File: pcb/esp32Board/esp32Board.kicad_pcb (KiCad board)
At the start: 4 copper layers, 38.2 x 42.1 mm, 31 parts, among them J1 ESPProgJTAG_RX, J10 USB_C_Receptacle_USB2.0, J2 ESPProg_RX, J3 ESPProgUART_RX, J4 CAN, J5 UART2, J6 I2C, J7 IO, J8 PWR, J9 GND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

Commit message: PCB Update
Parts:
- C2: value 20uF -> 22uF
- R2, R3, R8, R9: footprint Capacitor_SMD:C_0603_1608Metric -> Resistor_SMD:R_0603_1608Metric
- R4: value 2k -> 100k
- moved R1 0.94 mm to (145.2, 107.4)
- moved C2 0.49 mm to (145.2, 109.5)
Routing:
- net /EN: track 68.4 -> 84.0 mm
- net +3V3: track 93.0 -> 98.2 mm, vias 5 -> 4
- net GND: track 181.0 -> 181.6 mm

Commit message: Fix PCB Error
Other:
- board size 38.2 x 42.1 mm -> 38.2 x 41.1 mm
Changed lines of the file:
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@@
   (gr_line (start 146.4564 138.2522) (end 146.4564 142.5702) (layer "F.SilkS") (width 0.35))
   (gr_arc (start 138.8872 109.761573) (mid 140.058145 106.935942) (end 142.884027 105.7656) (layer "Edge.Cuts") (width 0.1))
-  (gr_line (start 177.0756 143.8728) (end 177.0756 109.743373) (layer "Edge.Cuts") (width 0.1))
+  (gr_line (start 177.0756 142.8728) (end 177.0756 109.743373) (layer "Edge.Cuts") (width 0.1))
   (gr_line (start 173.0756 105.743373) (end 142.884027 105.7656) (layer "Edge.Cuts") (width 0.1))
   (gr_arc (start 173.0756 105.743373) (mid 175.904027 106.914946) (end 177.0756 109.743373) (layer "Edge.Cuts") (width 0.1))
-  (gr_line (start 138.8872 109.761573) (end 138.8872 143.891) (layer "Edge.Cuts") (width 0.1))
-  (gr_arc (start 142.8872 147.891) (mid 140.058773 146.719427) (end 138.8872 143.891) (layer "Edge.Cuts") (width 0.1))
-  (gr_line (start 142.8872 147.891) (end 173.0756 147.8728) (layer "Edge.Cuts") (width 0.1))
-  (gr_arc (start 177.0756 143.8728) (mid 175.904027 146.701227) (end 173.0756 147.8728) (layer "Edge.Cuts") (width 0.1))
+  (gr_line (start 138.8872 109.761573) (end 138.8872 142.891) (layer "Edge.Cuts") (width 0.1))
+  (gr_arc (start 142.8872 146.891) (mid 140.058773 145.719427) (end 138.8872 142.891) (layer "Edge.Cuts") (width 0.1))
+  (gr_line (start 142.8872 146.891) (end 173.0756 146.8728) (layer "Edge.Cuts") (width 0.1))
+  (gr_arc (start 177.0756 142.8728) (mid 175.904027 145.701227) (end 173.0756 146.8728) (layer "Edge.Cuts") (width 0.1))
   (gr_text "JLCJLCJLCJLC" (at 158.115 108.458) (layer "B.SilkS")
     (effects (font (size 1 1) (thickness 0.15)) (justify mirror))

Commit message: PCB V0.2
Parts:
- removed J2: ESPProg_RX, Connector_Molex:Molex_CLIK-Mate_502382-1070_1x10-1MP_P1.25mm_Vertical
- removed R9: 0, Resistor_SMD:R_0603_1608Metric
- added D3: LED, LED_SMD:LED_0603_1608Metric, F.Cu at (146.1, 126.0)
- added J11: Conn_01x14_Female, Connector_PinHeader_2.54mm:PinHeader_1x14_P2.54mm_Vertical, F.Cu at (172.5, 108.8)
- added SW2: SW_Push_SPDT, KisonNew:0603JumperP3, F.Cu at (151.2, 129.5)
- added SW3: SW_Push_SPDT, KisonNew:0603JumperP3, F.Cu at (162.7, 133.4)
- added SW4: SW_Push_SPDT, KisonNew:0603JumperP3, F.Cu at (154.4, 129.3)
- J7: value IO -> InputOnly; footprint Connector_PinHeader_2.54mm:PinHeader_1x08_P2.54mm_Vertical -> Connector_PinHeader_2.54mm:PinHeader_1x04_P2.54mm_Vertical
- R4: value 100k -> 10k; moved to B.Cu
- R8: value 0 -> 10k; moved to B.Cu
- moved J7 32.2 mm to (142.1, 119.8), turned to 180 degrees
- moved J3 26.2 mm to (163.3, 109.8), turned to 180 degrees
- moved R8 25.4 mm to (143.3, 123.4), turned to -90 degrees
- moved J6 19.1 mm to (146.1, 119.0), turned to 0 degrees
- moved R4 18.4 mm to (141.5, 123.4), turned to -90 degrees
- moved D2 11.8 mm to (148.9, 132.2), turned to 180 degrees
- moved D1 10.3 mm to (146.1, 127.7)
- moved SW1 8.89 mm to (142.1, 128.3), turned to -90 degrees
- moved G*** 8.88 mm to (150.0, 131.5), turned to 0 degrees
- moved J1 8.78 mm to (150.9, 109.8), turned to 180 degrees
- moved C4 8.44 mm to (142.4, 128.6), turned to 0 degrees
- moved C6 8.17 mm to (159.5, 133.2), turned to -90 degrees
- moved R5 8.16 mm to (155.8, 145.0), turned to 0 degrees
- moved J8 7.27 mm to (144.0, 144.8), turned to 180 degrees
- moved R6 7.16 mm to (153.6, 141.6), turned to 0 degrees
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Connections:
- J4 pad 1: /CAN_VCC -> Net-(J4-Pad1)
- J7 pad 1: /IO23 -> /IO35
- J7 pad 2: /IO19 -> /IO34
- J7 pad 3: /IO18 -> /IO39
- J7 pad 4: /IO5 -> /IO36
- R8 pad 2: /CAN_VCC -> Net-(D3-Pad2)
- U1 pad 4: unconnected-(U1-Pad4) -> /IO36
- U1 pad 5: unconnected-(U1-Pad5) -> /IO39
- U1 pad 7: unconnected-(U1-Pad7) -> /IO35
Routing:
- net /EN: track 84.0 -> 46.4 mm, vias 3 -> 2
- net Net-(J11-Pad14): track 0.00 -> 26.5 mm, vias 0 -> 1
- net /IO5: track 6.75 -> 32.0 mm
- net /IO0: track 39.0 -> 14.0 mm
- net /RX: track 31.6 -> 9.22 mm, vias 2 -> 0
- net /EXT_5V: track 24.9 -> 46.2 mm, vias 0 -> 1
- net /TX: track 29.9 -> 12.3 mm, vias 2 -> 0
- net /SDA_IO25: track 20.9 -> 3.60 mm, vias 1 -> 0
- net /IO34: track 26.1 -> 8.95 mm, vias 1 -> 0
- net Net-(J4-Pad1): track 0.00 -> 16.0 mm, vias 0 -> 1
- net /TCLK: track 29.9 -> 15.2 mm, vias 2 -> 1
- net Net-(J11-Pad7): track 0.00 -> 13.9 mm, vias 0 -> 1
- net /SCL_IO26: track 18.0 -> 4.13 mm, vias 1 -> 0
- net /TMS: track 27.2 -> 14.2 mm, vias 2 -> 1
- net /IO32: track 24.4 -> 37.0 mm
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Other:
- board text added: "35"
- board text added: "36"
- board text added: "39"
- board text added: "GPPCB-V0.2"
- board text added: "InputOnly"
- board text added: "LED"
- board text added: "RX22"
- board text added: "TX21"
- board text added: "VCC"
- board text added: "屏幕朝向"
- board text removed: "RX_22"
- board text removed: "TX_21"

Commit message: Use XC6209 instead of trash XC6206
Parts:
- removed C6: 1uf, Capacitor_SMD:C_0603_1608Metric
- removed U2: XC6206P332MR, Package_TO_SOT_SMD:SOT-23
- added C10: 1uf, Capacitor_SMD:C_0603_1608Metric, F.Cu at (159.4, 133.3)
- added U3: XC6209, Package_TO_SOT_SMD:SOT-23-5, F.Cu at (156.2, 133.5)
- moved C5 0.59 mm to (153.1, 133.5)
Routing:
- net GND: track 175.5 -> 179.7 mm
- net /EXT_5V: track 46.2 -> 49.8 mm
- net Net-(D2-Pad2): track 18.2 -> 17.0 mm
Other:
- board text added: "GPPCB-V0.3"
- board text removed: "GPPCB-V0.2"

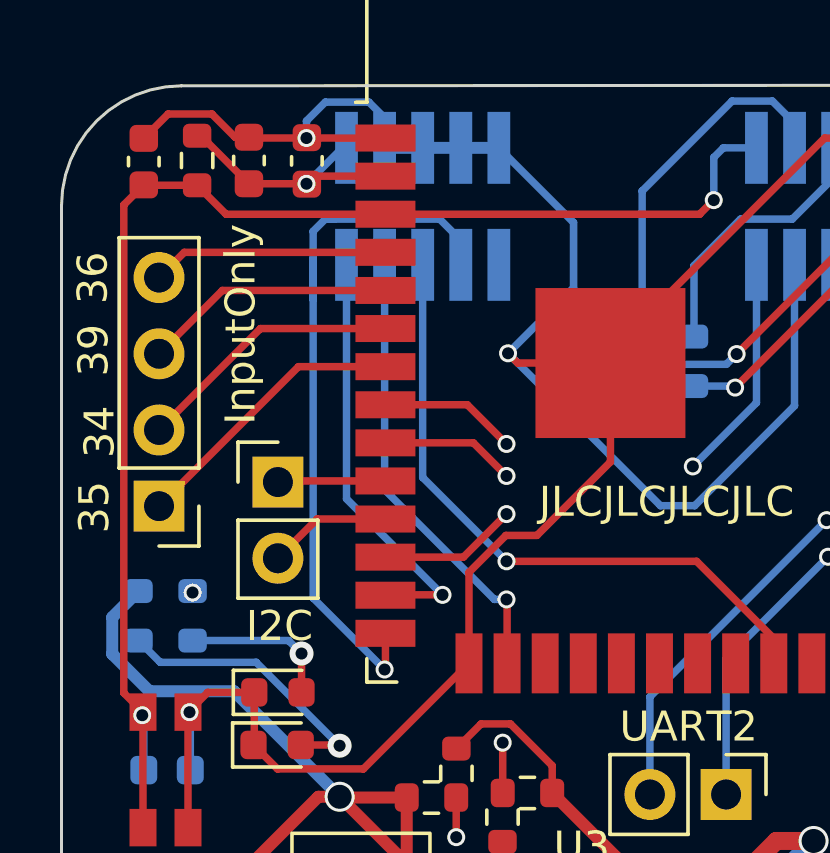
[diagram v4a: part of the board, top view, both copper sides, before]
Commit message: Fix I2C Pull Up
https://github.com/espressif/arduino-esp32/issues/3424 Damn why not design it strong enough so bad
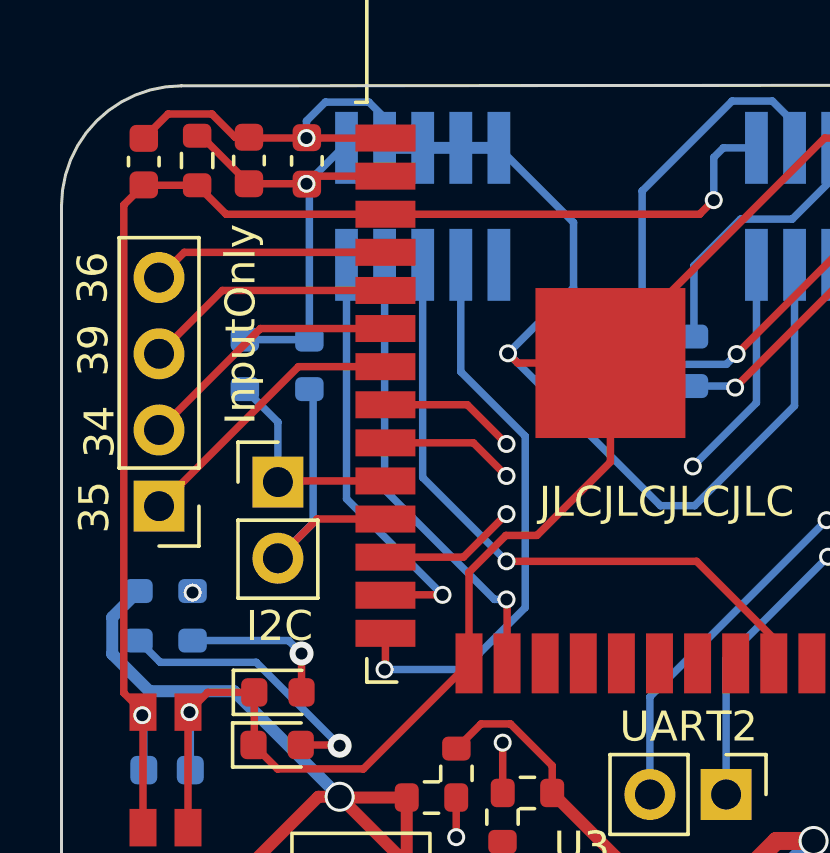
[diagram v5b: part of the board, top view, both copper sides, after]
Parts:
- added R10: 3.3k, Resistor_SMD:R_0603_1608Metric, B.Cu at (147.2, 115.0)
- added R9: 3.3k, Resistor_SMD:R_0603_1608Metric, B.Cu at (145.0, 115.0)
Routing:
- net +3V3: track 104.4 -> 111.8 mm
- net /SCL_IO26: track 4.13 -> 10.3 mm
- net /TDI: track 24.5 -> 19.9 mm
- net /SDA_IO25: track 3.60 -> 7.15 mm
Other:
- board text added: "GPPCB-V0.4"
- board text removed: "GPPCB-V0.3"
- board text removed: "屏幕朝向"
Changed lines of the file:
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@@
   )
   (footprint "Resistor_SMD:R_0603_1608Metric" (layer "B.Cu")
+    (at 145 115.05 -90)
+    (descr "Resistor SMD 0603 (1608 Metric), square (rectangular) end terminal, IPC_7351 nominal, (Body size source: IPC-SM-782 page 72, https://www.pcb-3d.com/wordpress/wp-content/uploads/ipc-sm-782a_amendment_1_and_2.pdf), generated with kicad-footprint-generator")
+    (tags "resistor")
+    (property "LCSC" "C429617")
+    (property "Sheetfile" "esp32Board.kicad_sch")
+    (property "Sheetname" "")
+    (attr smd)
+    (fp_text reference "R9" (at 0 1.43 90) (layer "B.SilkS")
+      (effects (font (size 1 1) (thickness 0.15)) (justify mirror))
+    )
+    (fp_text value "3.3k" (at 0 -1.43 90) (layer "B.Fab")
+      (effects (font (size 1 1) (thickness 0.15)) (justify mirror))
+    )
+    (fp_text user "${REFERENCE}" (at 0 0 90) (layer "B.Fab")
+      (effects (font (size 0.4 0.4) (thickness 0.06)) (justify mirror))
+    )
+    (fp_line (start -0.237258 0.5225) (end 0.237258 0.5225) (layer "B.SilkS") (width 0.12))
+    (fp_line (start -0.237258 -0.5225) (end 0.237258 -0.5225) (layer "B.SilkS") (width 0.12))
+    (fp_line (start 1.48 -0.73) (end -1.48 -0.73) (layer "B.CrtYd") (width 0.05))
+    (fp_line (start -1.48 -0.73) (end -1.48 0.73) (layer "B.CrtYd") (width 0.05))
+    (fp_line (start -1.48 0.73) (end 1.48 0.73) (layer "B.CrtYd") (width 0.05))
+    (fp_line (start 1.48 0.73) (end 1.48 -0.73) (layer "B.CrtYd") (width 0.05))
+    (fp_line (start -0.8 -0.4125) (end -0.8 0.4125) (layer "B.Fab") (width 0.1))
+    (fp_line (start 0.8 -0.4125) (end -0.8 -0.4125) (layer "B.Fab") (width 0.1))
+    (fp_line (start -0.8 0.4125) (end 0.8 0.4125) (layer "B.Fab") (width 0.1))
+    (fp_line (start 0.8 0.4125) (end 0.8 -0.4125) (layer "B.Fab") (width 0.1))
+    (pad "1" smd roundrect (at -0.825 0 270) (size 0.8 0.95) (layers "B.Cu" "B.Paste" "B.Mask") (roundrect_rratio 0.25)
+      (net 3 "+3V3") (pintype "passive"))
+    (pad "2" smd roundrect (at 0.825 0 270) (size 0.8 0.95) (layers "B.Cu" "B.Paste" "B.Mask") (roundrect_rratio 0.25)
+      (net 47 "/SDA_IO25") (pintype "passive"))
+    (model "${KICAD6_3DMODEL_DIR}/Resistor_SMD.3dshapes/R_0603_1608Metric.wrl"
+      (offset (xyz 0 0 0))
+      (scale (xyz 1 1 1))
+      (rotate (xyz 0 0 0))
+    )
+  )
+  (footprint "Resistor_SMD:R_0603_1608Metric" (layer "B.Cu")
     (at 155.8036 144.9832)
     (descr "Resistor SMD 0603 (1608 Metric), square (rectangular) end terminal, IPC_7351 nominal, (Body size source: IPC-SM-782 page 72, https://www.pcb-3d.com/wordpress/wp-content/uploads/ipc-sm-782a_amendment_1_and_2.pdf), generated with kicad-footprint-generator")
@@
       ) (layer "B.SilkS") (width 0) (fill solid))
   )
+  (footprint "Resistor_SMD:R_0603_1608Metric" (layer "B.Cu")
+    (at 147.15 115.05 -90)
+    (descr "Resistor SMD 0603 (1608 Metric), square (rectangular) end terminal, IPC_7351 nominal, (Body size source: IPC-SM-782 page 72, https://www.pcb-3d.com/wordpress/wp-content/uploads/ipc-sm-782a_amendment_1_and_2.pdf), generated with kicad-footprint-generator")
+    (tags "resistor")
+    (property "LCSC" "C429617")
+    (property "Sheetfile" "esp32Board.kicad_sch")
+    (property "Sheetname" "")
+    (attr smd)
+    (fp_text reference "R10" (at 0 1.43 90) (layer "B.SilkS")
+      (effects (font (size 1 1) (thickness 0.15)) (justify mirror))
+    )
+    (fp_text value "3.3k" (at 0 -1.43 90) (layer "B.Fab")
+      (effects (font (size 1 1) (thickness 0.15)) (justify mirror))
+    )
+    (fp_text user "${REFERENCE}" (at 0 0 90) (layer "B.Fab")
+      (effects (font (size 0.4 0.4) (thickness 0.06)) (justify mirror))
+    )
+    (fp_line (start -0.237258 -0.5225) (end 0.237258 -0.5225) (layer "B.SilkS") (width 0.12))
+    (fp_line (start -0.237258 0.5225) (end 0.237258 0.5225) (layer "B.SilkS") (width 0.12))
+    (fp_line (start -1.48 0.73) (end 1.48 0.73) (layer "B.CrtYd") (width 0.05))
+    (fp_line (start -1.48 -0.73) (end -1.48 0.73) (layer "B.CrtYd") (width 0.05))
+    (fp_line (start 1.48 0.73) (end 1.48 -0.73) (layer "B.CrtYd") (width 0.05))
+    (fp_line (start 1.48 -0.73) (end -1.48 -0.73) (layer "B.CrtYd") (width 0.05))
+    (fp_line (start -0.8 0.4125) (end 0.8 0.4125) (layer "B.Fab") (width 0.1))
+    (fp_line (start 0.8 -0.4125) (end -0.8 -0.4125) (layer "B.Fab") (width 0.1))
+    (fp_line (start 0.8 0.4125) (end 0.8 -0.4125) (layer "B.Fab") (width 0.1))
+    (fp_line (start -0.8 -0.4125) (end -0.8 0.4125) (layer "B.Fab") (width 0.1))
+    (pad "1" smd roundrect (at -0.825 0 270) (size 0.8 0.95) (layers "B.Cu" "B.Paste" "B.Mask") (roundrect_rratio 0.25)
+      (net 3 "+3V3") (pintype "passive"))
+    (pad "2" smd roundrect (at 0.825 0 270) (size 0.8 0.95) (layers "B.Cu" "B.Paste" "B.Mask") (roundrect_rratio 0.25)
+      (net 48 "/SCL_IO26") (pintype "passive"))
+    (model "${KICAD6_3DMODEL_DIR}/Resistor_SMD.3dshapes/R_0603_1608Metric.wrl"
+      (offset (xyz 0 0 0))
+      (scale (xyz 1 1 1))
+      (rotate (xyz 0 0 0))
+    )
+  )
   (footprint "KisonNew:IDC_1.27mm_10P" (layer "B.Cu")
     (at 150.9268 109.7832 180)
@@
     (effects (font (size 1 1) (thickness 0.15)) (justify mirror))
   )
-  (gr_text "屏幕朝向" (at 175.4124 122.4026 90) (layer "B.SilkS")
-    (effects (font (size 3 3) (thickness 0.15)) (justify mirror))
-  )
-  (gr_text "GPPCB-V0.3" (at 141.3002 140.0302 90) (layer "B.SilkS")
+  (gr_text "GPPCB-V0.4" (at 141.3002 140.0302 90) (layer "B.SilkS")
     (effects (font (size 1 1) (thickness 0.15)) (justify mirror))
   )
@@
   (segment (start 145.392911 135.800489) (end 144.0434 137.15) (width 0.6) (layer "B.Cu") (net 3))
   (segment (start 162.052 111.7332) (end 162.052 116.332) (width 0.25) (layer "B.Cu") (net 3))
+  (segment (start 147.15 109.1268) (end 147.053 109.0298) (width 0.25) (layer "B.Cu") (net 3))
+  (segment (start 147.15 114.225) (end 147.15 109.1268) (width 0.25) (layer "B.Cu") (net 3))
   (segment (start 163.957 130.937) (end 159.093511 135.800489) (width 0.6) (layer "B.Cu") (net 3))
   (segment (start 162.052 116.332) (end 159.9311 118.4529) (width 0.25) (layer "B.Cu") (net 3))
+  (segment (start 145 114.225) (end 147.15 114.225) (width 0.25) (layer "B.Cu") (net 3))
   (segment (start 148.2496 107.8332) (end 147.053 109.0298) (width 0.25) (layer "B.Cu") (net 3))
   (segment (start 144.0434 139.69) (end 144.0434 137.15) (width 1) (layer "B.Cu") (net 3))
@@
   (segment (start 149.685 124.0164) (end 149.685 125.1938) (width 0.25) (layer "F.Cu") (net 17))
   (via (at 149.6568 125.222) (size 0.6) (drill 0.4) (layers "F.Cu" "B.Cu") (net 17))
-  (segment (start 147.682289 110.208689) (end 148.003889 110.208689) (width 0.25) (layer "B.Cu") (net 17))
-  (segment (start 147.275311 122.840511) (end 149.6568 125.222) (width 0.25) (layer "B.Cu") (net 17))
-  (segment (start 147.275311 112.883711) (end 147.275311 122.840511) (width 0.25) (layer "B.Cu") (net 17))
-  (segment (start 147.275311 111.512111) (end 147.275311 112.883711) (width 0.25) (layer "B.Cu") (net 17))
-  (segment (start 152.1968 110.9132) (end 151.492289 110.208689) (width 0.25) (layer "B.Cu") (net 17))
+  (segment (start 152.1968 115.296407) (end 154.345311 117.444918) (width 0.25) (layer "B.Cu") (net 17))
+  (segment (start 154.345311 117.444918) (end 154.345311 123.154689) (width 0.25) (layer "B.Cu") (net 17))
+  (segment (start 152.278 125.222) (end 149.6568 125.222) (width 0.25) (layer "B.Cu") (net 17))
   (segment (start 152.1968 111.7332) (end 152.1968 110.9132) (width 0.25) (layer "B.Cu") (net 17))
-  (segment (start 147.275311 112.883711) (end 147.275311 110.615667) (width 0.25) (layer "B.Cu") (net 17))
-  (segment (start 147.275311 110.615667) (end 147.682289 110.208689) (width 0.25) (layer "B.Cu") (net 17))
-  (segment (start 151.492289 110.208689) (end 147.855311 110.208689) (width 0.25) (layer "B.Cu") (net 17))
+  (segment (start 152.1968 111.7332) (end 152.1968 115.296407) (width 0.25) (layer "B.Cu") (net 17))
+  (segment (start 154.345311 123.154689) (end 152.278 125.222) (width 0.25) (layer "B.Cu") (net 17))
   (segment (start 153.74 122.9044) (end 153.7208 122.8852) (width 0.25) (layer "F.Cu") (net 18))
   (segment (start 153.74 125.0164) (end 153.74 122.9044) (width 0.25) (layer "F.Cu") (net 18))
@@
   (segment (start 149.685 118.9364) (end 146.138 118.9364) (width 0.25) (layer "F.Cu") (net 47))
   (segment (start 146.138 118.9364) (end 146.1008 118.9736) (width 0.25) (layer "F.Cu") (net 47))
+  (segment (start 145 115.875) (end 146.1008 116.9758) (width 0.25) (layer "B.Cu") (net 47))
+  (segment (start 146.1008 116.9758) (end 146.1008 118.9736) (width 0.25) (layer "B.Cu") (net 47))
   (segment (start 147.408 120.2064) (end 146.1008 121.5136) (width 0.25) (layer "F.Cu") (net 48))
   (segment (start 149.685 120.2064) (end 147.408 120.2064) (width 0.25) (layer "F.Cu") (net 48))
+  (segment (start 147.15 115.875) (end 147.275311 116.000311) (width 0.25) (layer "B.Cu") (net 48))
+  (segment (start 147.275311 120.339089) (end 146.1008 121.5136) (width 0.25) (layer "B.Cu") (net 48))
+  (segment (start 147.275311 116.000311) (end 147.275311 120.339089) (width 0.25) (layer "B.Cu") (net 48))
   (segment (start 166.685 121.4764) (end 164.4532 121.4764) (width 0.25) (layer "F.Cu") (net 49))
   (segment (start 164.4532 121.4764) (end 164.4396 121.4628) (width 0.25) (layer "F.Cu") (net 49))
